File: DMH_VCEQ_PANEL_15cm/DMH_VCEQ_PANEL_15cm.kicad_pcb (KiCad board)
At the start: 2 copper layers, 150 x 200 mm, 8 parts

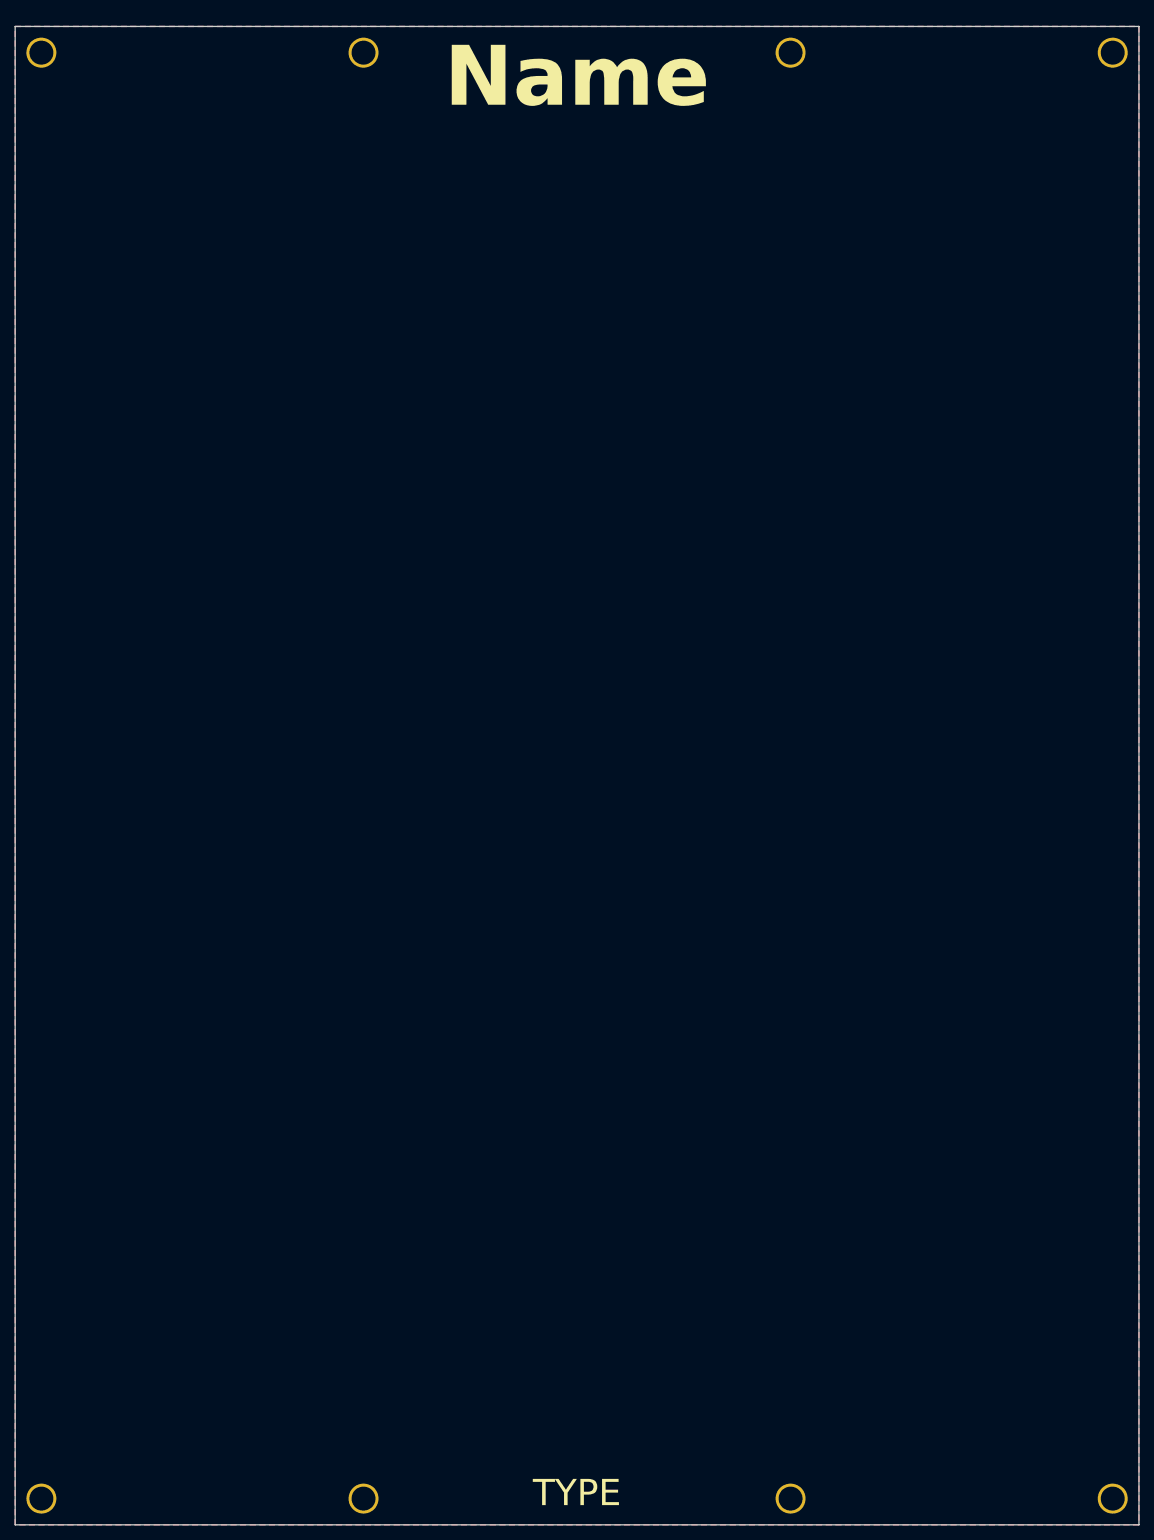
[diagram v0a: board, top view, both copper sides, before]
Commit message: Designed 15cm panel version
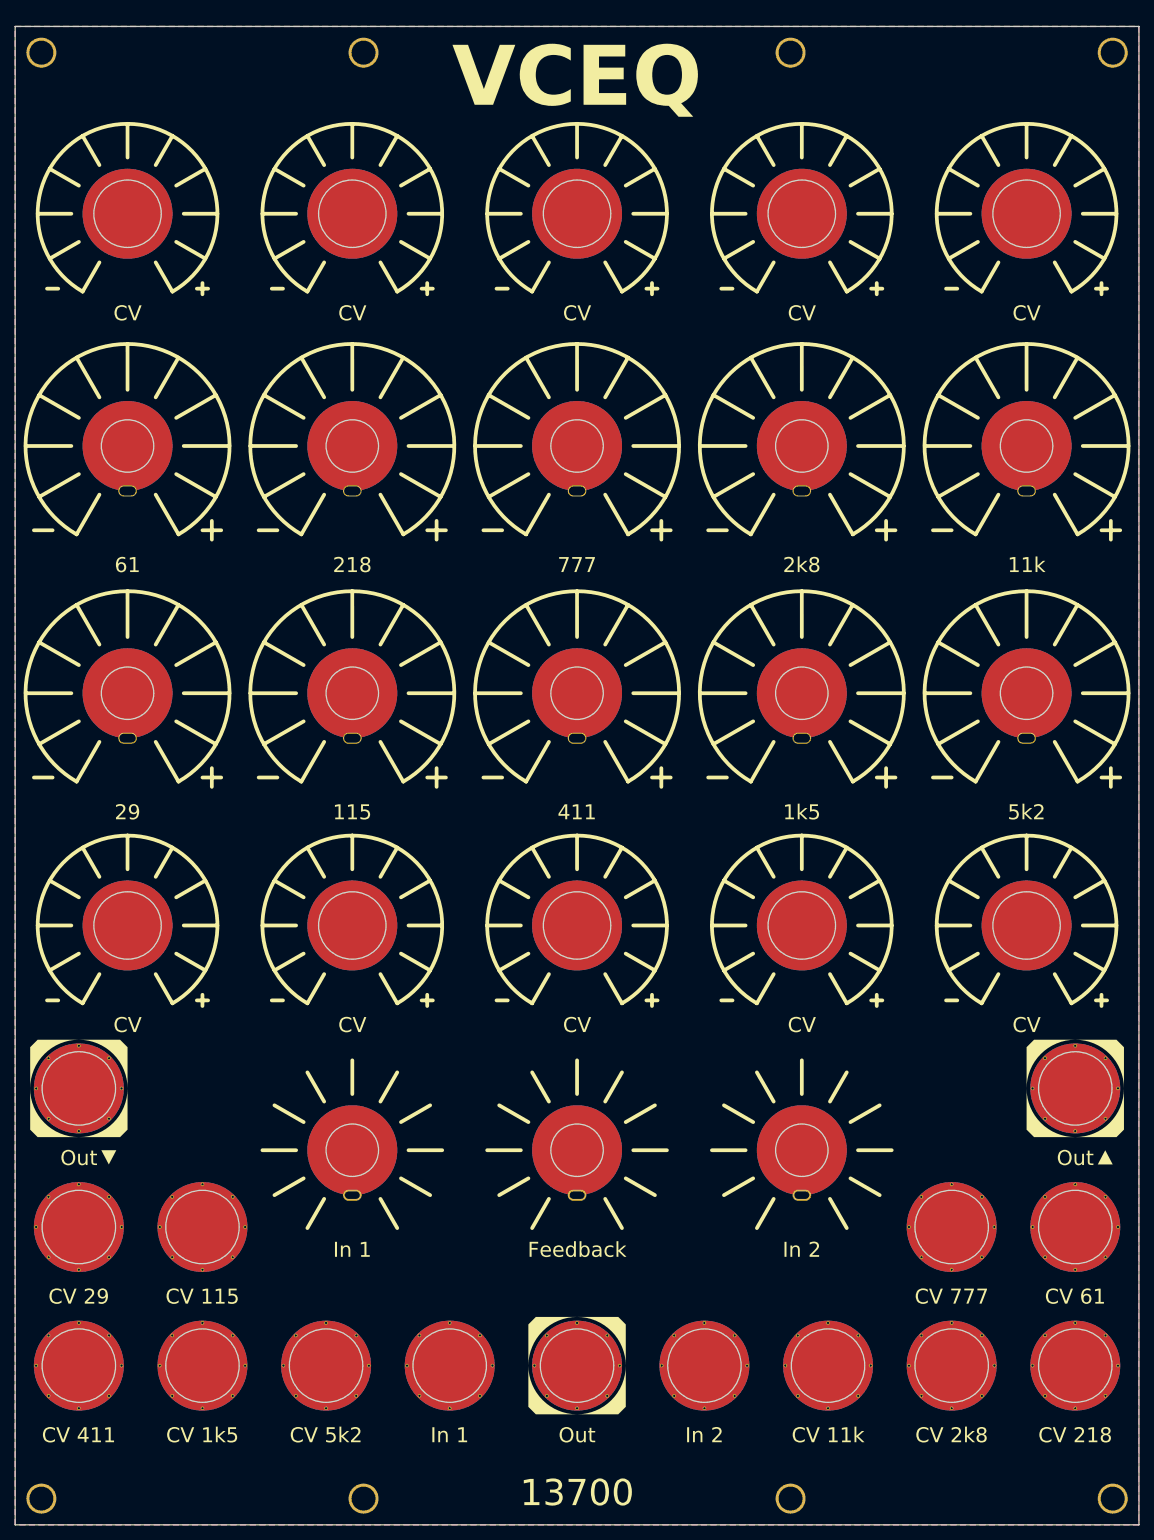
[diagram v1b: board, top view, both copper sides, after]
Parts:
- added H10: 29, SynthStuff:Pot_Cutout_Small_attv_RD901F, F.Cu at (40.0, 119.0)
- added H11: 115, SynthStuff:Pot_Cutout_Small_attv_RD901F, F.Cu at (70.0, 119.0)
- added H12: 411, SynthStuff:Pot_Cutout_Small_attv_RD901F, F.Cu at (100.0, 119.0)
- added H13: 1k5, SynthStuff:Pot_Cutout_Small_attv_RD901F, F.Cu at (130.0, 119.0)
- added H14: 5k2, SynthStuff:Pot_Cutout_Small_attv_RD901F, F.Cu at (160.0, 119.0)
- added H15: CV, SynthStuff:Pot_Cutout_Tiny_attv_P110KH1, F.Cu at (40.0, 55.0)
- added H16: CV, SynthStuff:Pot_Cutout_Tiny_attv_P110KH1, F.Cu at (70.0, 55.0)
- added H17: CV, SynthStuff:Pot_Cutout_Tiny_attv_P110KH1, F.Cu at (100.0, 55.0)
- added H18: CV, SynthStuff:Pot_Cutout_Tiny_attv_P110KH1, F.Cu at (130.0, 55.0)
- added H19: CV, SynthStuff:Pot_Cutout_Tiny_attv_P110KH1, F.Cu at (160.0, 55.0)
- added H20: CV, SynthStuff:Pot_Cutout_Tiny_attv_P110KH1, F.Cu at (40.0, 150.0)
- added H21: CV, SynthStuff:Pot_Cutout_Tiny_attv_P110KH1, F.Cu at (70.0, 150.0)
- added H22: CV, SynthStuff:Pot_Cutout_Tiny_attv_P110KH1, F.Cu at (100.0, 150.0)
- added H23: CV, SynthStuff:Pot_Cutout_Tiny_attv_P110KH1, F.Cu at (130.0, 150.0)
- added H24: CV, SynthStuff:Pot_Cutout_Tiny_attv_P110KH1, F.Cu at (160.0, 150.0)
- added H25: In 1, SynthStuff:Pot_Cutout_Tiny, F.Cu at (70.0, 180.0)
- added H26: In 2, SynthStuff:Pot_Cutout_Tiny, F.Cu at (130.0, 180.0)
- added H27: Feedback, SynthStuff:Pot_Cutout_Tiny, F.Cu at (100.0, 180.0)
- added H28: In 1, SynthStuff:Jack_6.35mm_Cutout_v3, F.Cu at (83.0, 208.8)
- added H29: In 2, SynthStuff:Jack_6.35mm_Cutout_v3, F.Cu at (117.0, 208.8)
- added H30: Out, SynthStuff:Jack_6.35mm_Cutout_Output_v6, F.Cu at (33.5, 171.8)
- added H31: Out, SynthStuff:Jack_6.35mm_Cutout_Output_v6, F.Cu at (166.5, 171.8)
- added H32: Out, SynthStuff:Jack_6.35mm_Cutout_Output_v6, F.Cu at (100.0, 208.8)
- added H33: CV 61, SynthStuff:Jack_6.35mm_Cutout_v3, F.Cu at (166.5, 190.2)
- added H34: CV 218, SynthStuff:Jack_6.35mm_Cutout_v3, F.Cu at (166.5, 208.8)
- added H35: CV 777, SynthStuff:Jack_6.35mm_Cutout_v3, F.Cu at (150.0, 190.2)
- added H36: CV 2k8, SynthStuff:Jack_6.35mm_Cutout_v3, F.Cu at (150.0, 208.8)
- added H37: CV 11k, SynthStuff:Jack_6.35mm_Cutout_v3, F.Cu at (133.5, 208.8)
- added H38: CV 29, SynthStuff:Jack_6.35mm_Cutout_v3, F.Cu at (33.5, 190.2)
- added H39: CV 115, SynthStuff:Jack_6.35mm_Cutout_v3, F.Cu at (50.0, 190.2)
- added H40: CV 411, SynthStuff:Jack_6.35mm_Cutout_v3, F.Cu at (33.5, 208.8)
- added H41: CV 1k5, SynthStuff:Jack_6.35mm_Cutout_v3, F.Cu at (50.0, 208.8)
- added H42: CV 5k2, SynthStuff:Jack_6.35mm_Cutout_v3, F.Cu at (66.5, 208.8)
- added H5: 61, SynthStuff:Pot_Cutout_Small_attv_RD901F, F.Cu at (40.0, 86.0)
- added H6: 218, SynthStuff:Pot_Cutout_Small_attv_RD901F, F.Cu at (70.0, 86.0)
- added H7: 777, SynthStuff:Pot_Cutout_Small_attv_RD901F, F.Cu at (100.0, 86.0)
- added H8: 2k8, SynthStuff:Pot_Cutout_Small_attv_RD901F, F.Cu at (130.0, 86.0)
- added H9: 11k, SynthStuff:Pot_Cutout_Small_attv_RD901F, F.Cu at (160.0, 86.0)
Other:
- board text added: "13700"
- board text added: "VCEQ"
- board text removed: "Name"
- board text removed: "TYPE"

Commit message: Added FB/DW and M/S features
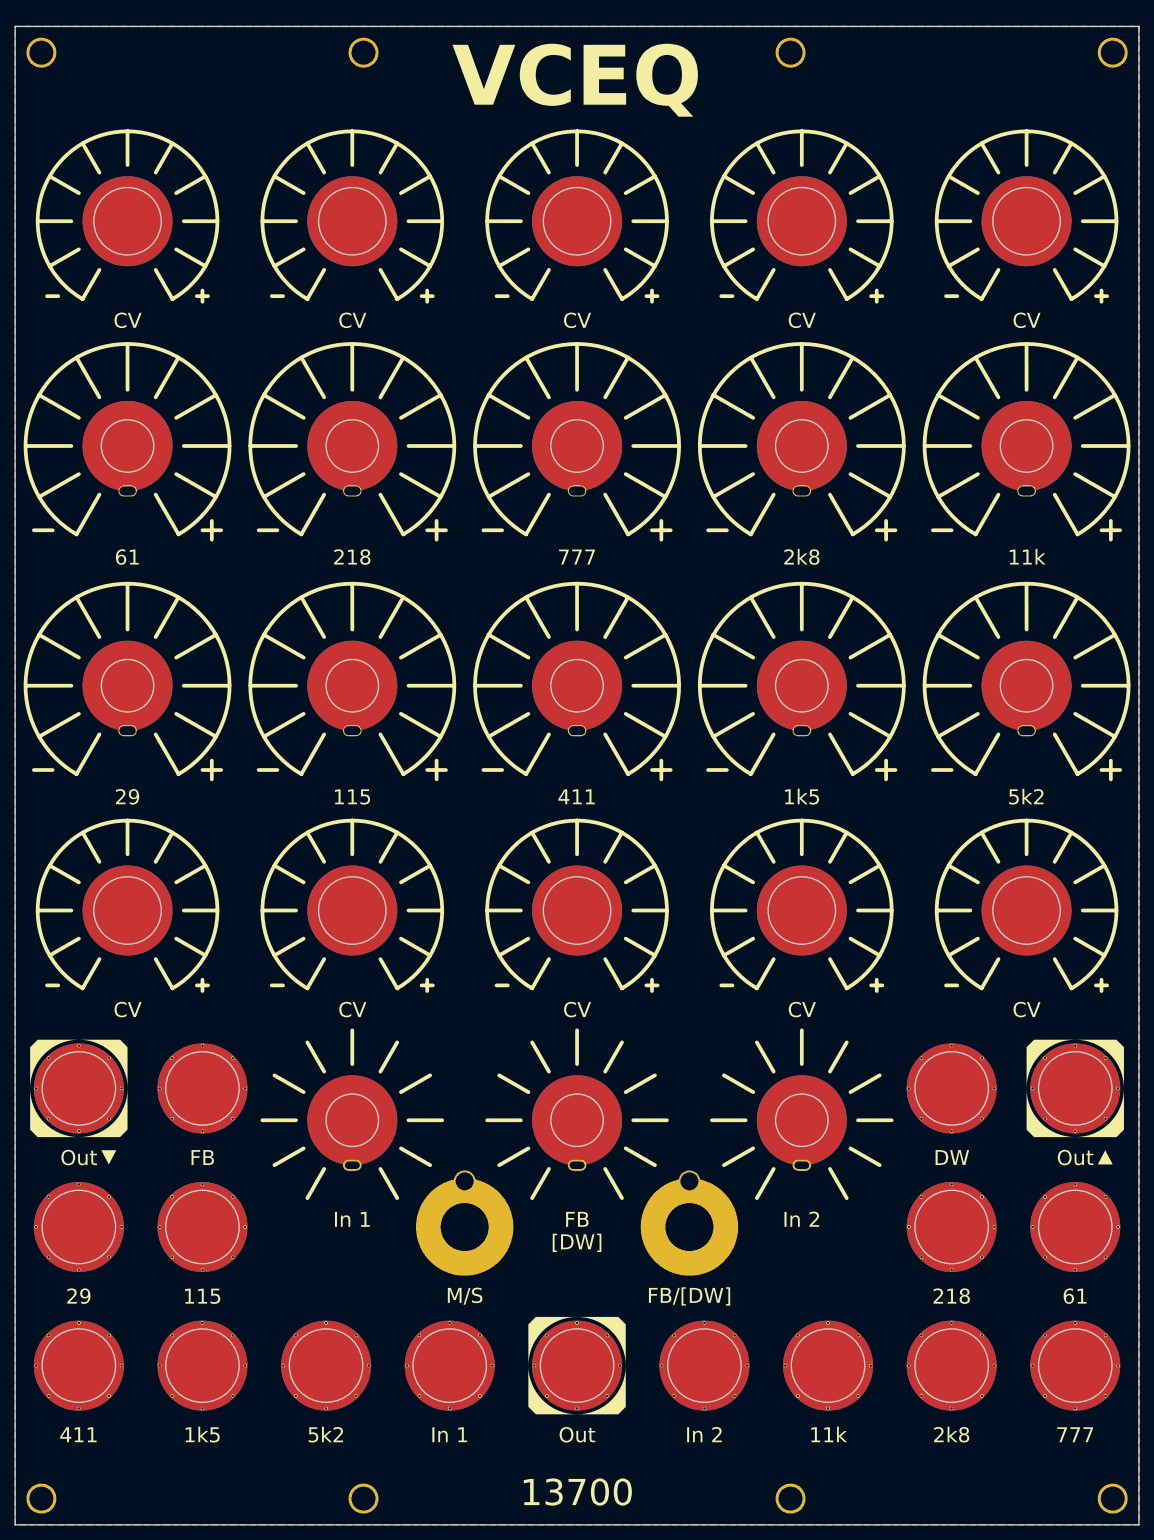
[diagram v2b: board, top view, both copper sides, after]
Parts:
- added H57: M/S, SynthStuff:Toggle_Switch_TE_Cutout, F.Cu at (85.0, 190.2)
- added H58: FB/[DW], SynthStuff:Toggle_Switch_TE_Cutout, F.Cu at (115.0, 190.2)
- added H59: FB, SynthStuff:Jack_6.35mm_Cutout_v3, F.Cu at (50.0, 171.8)
- added H60: DW, SynthStuff:Jack_6.35mm_Cutout_v3, F.Cu at (150.0, 171.8)
- H27: value Feedback -> FB
- H33: value CV 61 -> 61
- H34: value CV 218 -> 218
- H35: value CV 777 -> 777
- H36: value CV 2k8 -> 2k8
- H37: value CV 11k -> 11k
- H38: value CV 29 -> 29
- H39: value CV 115 -> 115
- H40: value CV 411 -> 411
- H41: value CV 1k5 -> 1k5
- H42: value CV 5k2 -> 5k2
- moved H34 24.8 mm to (150.0, 190.2)
- moved H35 24.8 mm to (166.5, 208.8)
- moved H25 4.00 mm to (70.0, 176.0)
- moved H26 4.00 mm to (130.0, 176.0)
- moved H27 4.00 mm to (100.0, 176.0)
- moved H20 2.00 mm to (40.0, 148.0)
- moved H21 2.00 mm to (70.0, 148.0)
- moved H22 2.00 mm to (100.0, 148.0)
- moved H23 2.00 mm to (130.0, 148.0)
- moved H24 2.00 mm to (160.0, 148.0)
- moved H10 1.00 mm to (40.0, 118.0)
- moved H11 1.00 mm to (70.0, 118.0)
- moved H12 1.00 mm to (100.0, 118.0)
- moved H13 1.00 mm to (130.0, 118.0)
- moved H14 1.00 mm to (160.0, 118.0)
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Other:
- board text added: "[DW]"

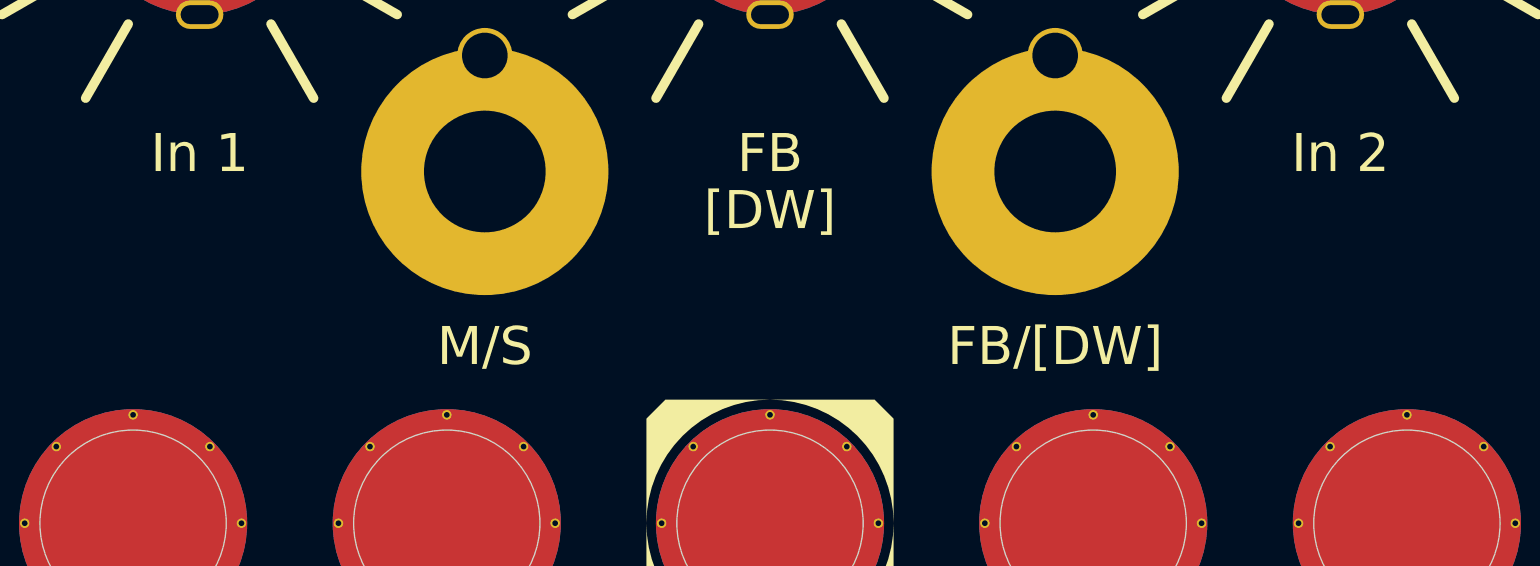
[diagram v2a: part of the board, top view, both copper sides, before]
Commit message: Finished 15 and 10 panels
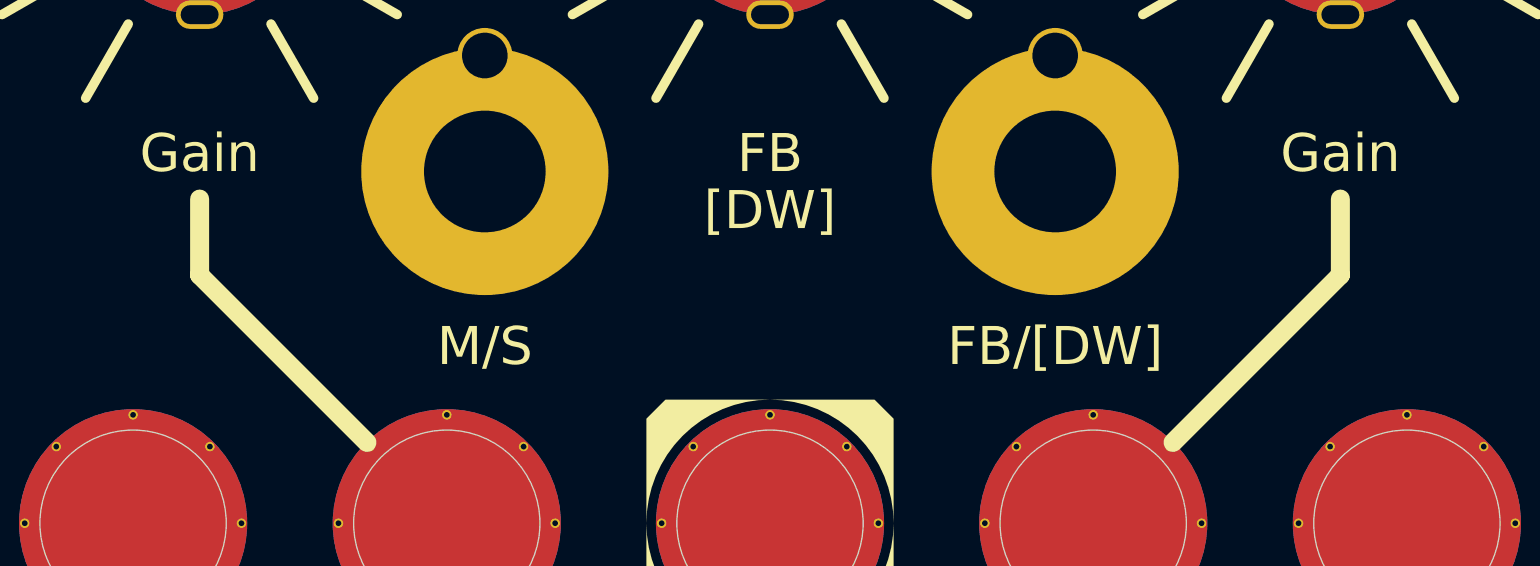
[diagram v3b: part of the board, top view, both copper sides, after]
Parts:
- H25: value In 1 -> Gain
- H26: value In 2 -> Gain
